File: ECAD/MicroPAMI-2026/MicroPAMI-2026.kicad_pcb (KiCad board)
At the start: 2 copper layers, 54 x 60 mm, 35 parts, among them J1 Conn_01x05, J13 OLED, J2 Conn_01x05, J3 MicroServo 2G, J5 UPDI, SW2 Left, SW3 Right, SW4 SW_SPDT, SW5 SW_DIP_x01, U1 ATtiny3226-S, U2 ITR9608-F, U4 AMS1117-5.0, U5 ULN2803A

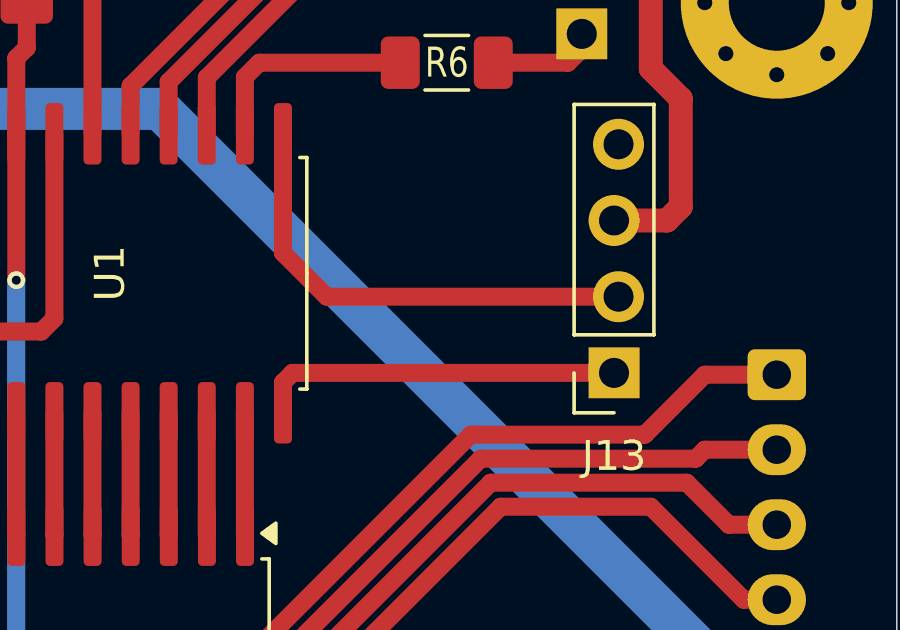
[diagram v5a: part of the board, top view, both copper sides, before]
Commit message: add I2C resistor
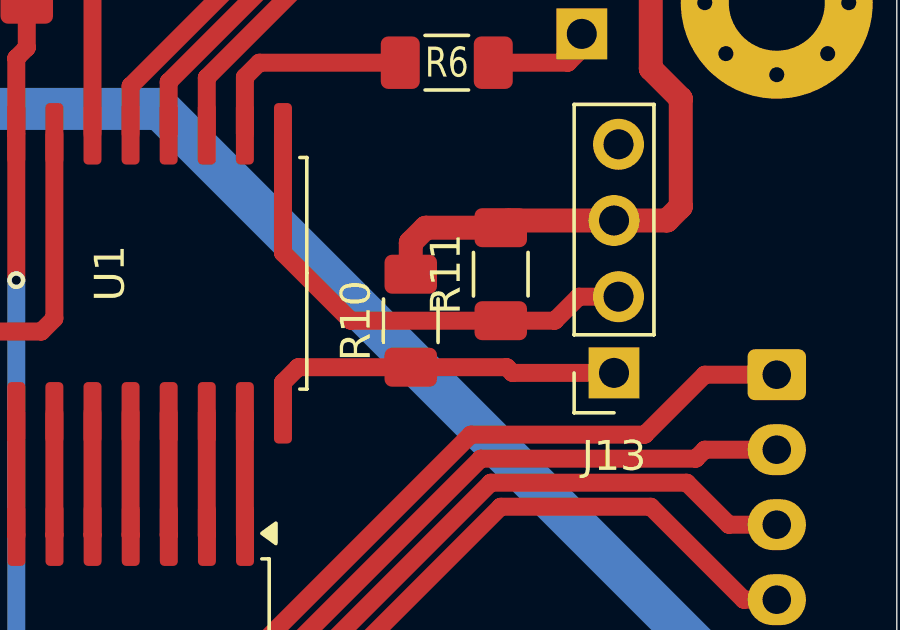
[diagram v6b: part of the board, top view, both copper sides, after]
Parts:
- added R10: 4K7, Resistor_SMD:R_1206_3216Metric_Pad1.30x1.75mm_HandSolder, F.Cu at (90.8, 95.6)
- added R11: 4K7, Resistor_SMD:R_1206_3216Metric_Pad1.30x1.75mm_HandSolder, F.Cu at (93.8, 94.0)
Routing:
- net +5V: track 136.2 -> 144.3 mm
- net SCL: track 15.6 -> 16.3 mm

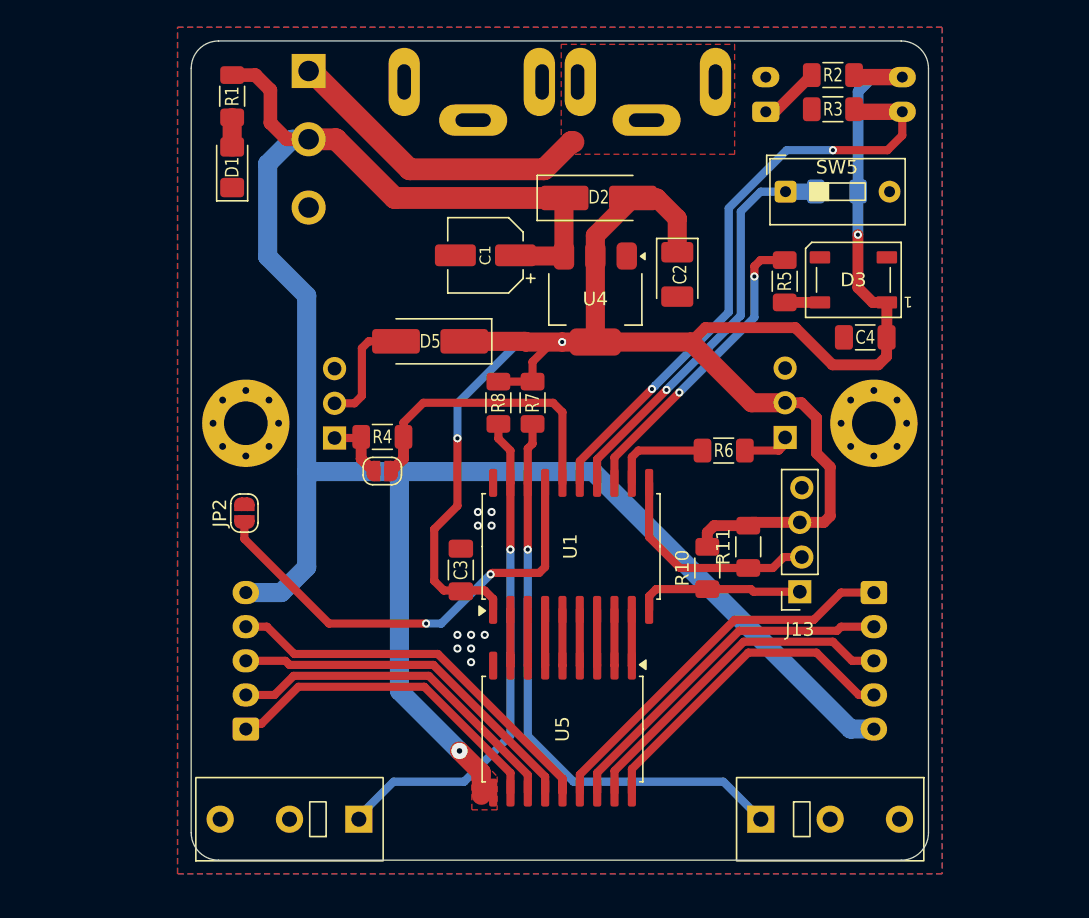
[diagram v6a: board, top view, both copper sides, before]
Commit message: add pogo for programming
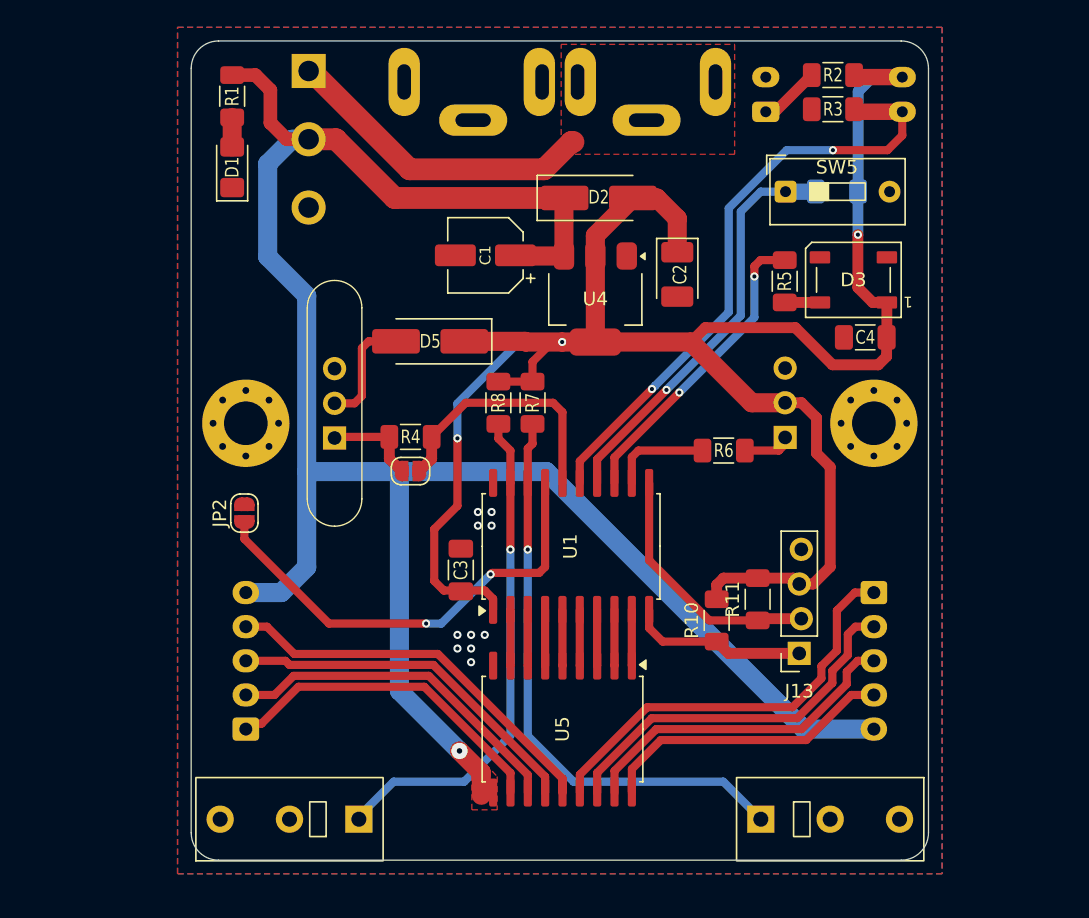
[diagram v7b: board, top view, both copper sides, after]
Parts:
- moved J13 4.51 mm to (97.5, 101.9)
- moved R10 3.90 mm to (91.5, 99.4)
- moved R11 3.90 mm to (94.5, 97.9)
- moved JP1 2.06 mm to (69.1, 88.5)
- moved R4 2.06 mm to (69.1, 86.0)
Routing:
- net +5V: track 144.3 -> 147.8 mm
- net /UPDI: track 21.6 -> 19.0 mm
- net Net-(J2-Pin_4): track 24.3 -> 21.7 mm
- net Net-(J2-Pin_1): track 28.4 -> 30.9 mm
- net SCL: track 16.3 -> 18.7 mm
- net Net-(J5-Pin_1): track 4.86 -> 6.92 mm
- net Net-(J2-Pin_2): track 26.1 -> 27.9 mm
- net SDA: track 12.3 -> 13.1 mm
- net Net-(J2-Pin_3): track 25.1 -> 24.4 mm

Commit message: update to production POC
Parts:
- added G***: LOGO, LOGO, B.Cu at (101.7, 75.9)
- added G***: LOGO, LOGO, B.Cu at (59.8, 75.4)
- moved D5 1.01 mm to (71.5, 79.1)
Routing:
- net Net-(D5-A): track 8.43 -> 9.48 mm
- net +5V: track 147.8 -> 146.8 mm
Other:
- board text added: "Sig"
